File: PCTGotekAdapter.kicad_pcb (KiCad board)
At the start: 2 copper layers, 114.3 x 55.9 mm, 21 parts, among them J1 Conn_02x17_Odd_Even, J2 Conn_2Rows-19Pins, J3 Conn_2Rows-19Pins, J4 Conn_02x17_Odd_Even, J5 Conn_01x04_Pin, J6 Conn_01x04_Pin, U1 SN74LS138N, U2 SN7407N

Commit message: First pass at REV B
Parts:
- removed J3: Conn_2Rows-19Pins, Connector_PinHeader_2.54mm:PinHeader_2x10_P2.54mm_Vertical
- moved R3 130.2 mm to (175.3, 99.1), turned to 90 degrees
- moved U1 128.1 mm to (189.4, 87.6), turned to 180 degrees
- moved R4 121.5 mm to (162.6, 99.1)
- moved H1 108.3 mm to (130.4, 77.9)
- moved H2 107.8 mm to (130.4, 118.5)
- moved J2 107.0 mm to (203.2, 109.2), turned to 180 degrees
- moved TP1 106.3 mm to (128.1, 96.5)
- moved J5 106.0 mm to (127.1, 90.0)
- moved J6 105.0 mm to (127.1, 109.2)
- moved J1 103.1 mm to (182.9, 116.8)
- moved J4 102.7 mm to (182.9, 104.1)
- moved TP2 101.3 mm to (133.2, 96.5)
- moved TP3 98.8 mm to (138.2, 96.5)
- moved R1 95.0 mm to (169.0, 99.1), turned to 90 degrees
- moved C2 94.1 mm to (182.5, 96.5), turned to 180 degrees
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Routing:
- net +5V: track 278.0 -> 140.7 mm, vias 3 -> 1
- net Net-(J1-Pin_16): track 159.0 -> 31.6 mm
- net Net-(J1-Pin_24): track 120.5 -> 32.7 mm
- net Net-(J2-Pin_17): track 99.3 -> 11.9 mm, vias 2 -> 0
- net Net-(J1-Pin_20): track 107.3 -> 42.2 mm, vias 0 -> 2
- net Net-(J2-Pin_4): track 85.1 -> 21.1 mm
- net Net-(J1-Pin_18): track 97.3 -> 40.3 mm
- net Net-(J2-Pin_9): track 62.9 -> 10.9 mm, vias 1 -> 0
- net Net-(J1-Pin_32): track 96.4 -> 45.9 mm
- net Net-(J1-Pin_26): track 121.4 -> 86.7 mm, vias 2 -> 1
- net Net-(J1-Pin_22): track 89.9 -> 55.9 mm, vias 2 -> 0
- net Net-(J2-Pin_5): track 28.4 -> 54.0 mm, vias 0 -> 4
- net Net-(J1-Pin_30): track 121.3 -> 97.1 mm
- net Net-(J2-Pin_12): track 35.8 -> 59.9 mm, vias 0 -> 3
- net Net-(J2-Pin_16): track 26.0 -> 47.3 mm, vias 0 -> 1
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- added copper zone on In1.Cu, net GND
- added copper zone on In2.Cu, net GND
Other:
- board size 114.3 x 55.9 mm -> 86.4 x 50.8 mm
- copper layers 2 -> 4
- board text added: "Connect Me to Your PC Transporter"
- board text added: "Copyright ©️ 2023 / CC BY SA"
- board text added: "LOT JLCJLCJLCJLC"
- board text added: "MS DOS Drive Connectors Maximum 2 drives - addressed by jumpers Power Performance Not Guaranteed"
- board text added: "PC Transporter GoDrive"
- board text added: "REV B"
- board text removed: "MS DOS Drive Connectors Maximum 2 drives - addressed by jumpers"
- board text removed: "PC Transporter Connectors Maximum 1 Connection"
- board text removed: "PC Transporter to MS DOS Drive Adapter"
- board text removed: "REV ${Rev} LOT JLCJLCJLCJLC"

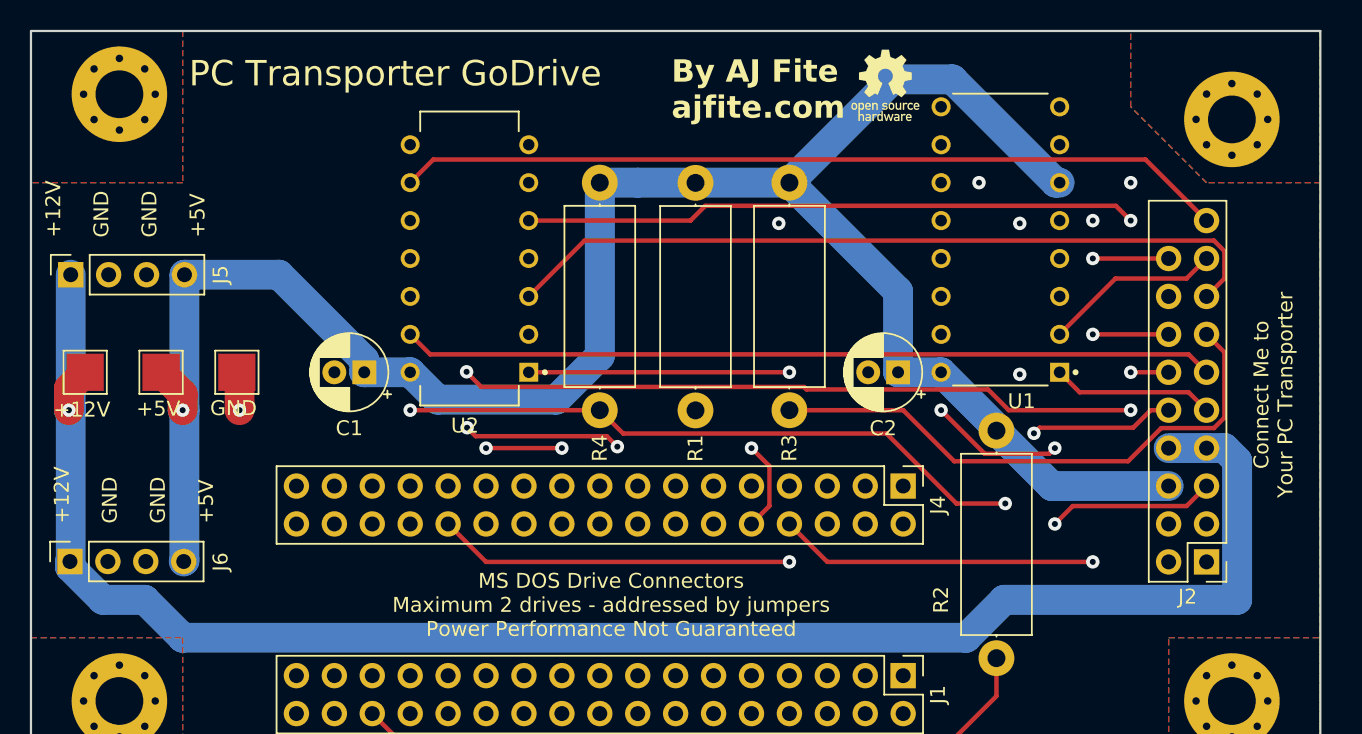
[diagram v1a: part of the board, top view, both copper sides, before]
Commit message: Remove extraneous connector from schematic
Also some silkscreen and path tweaks
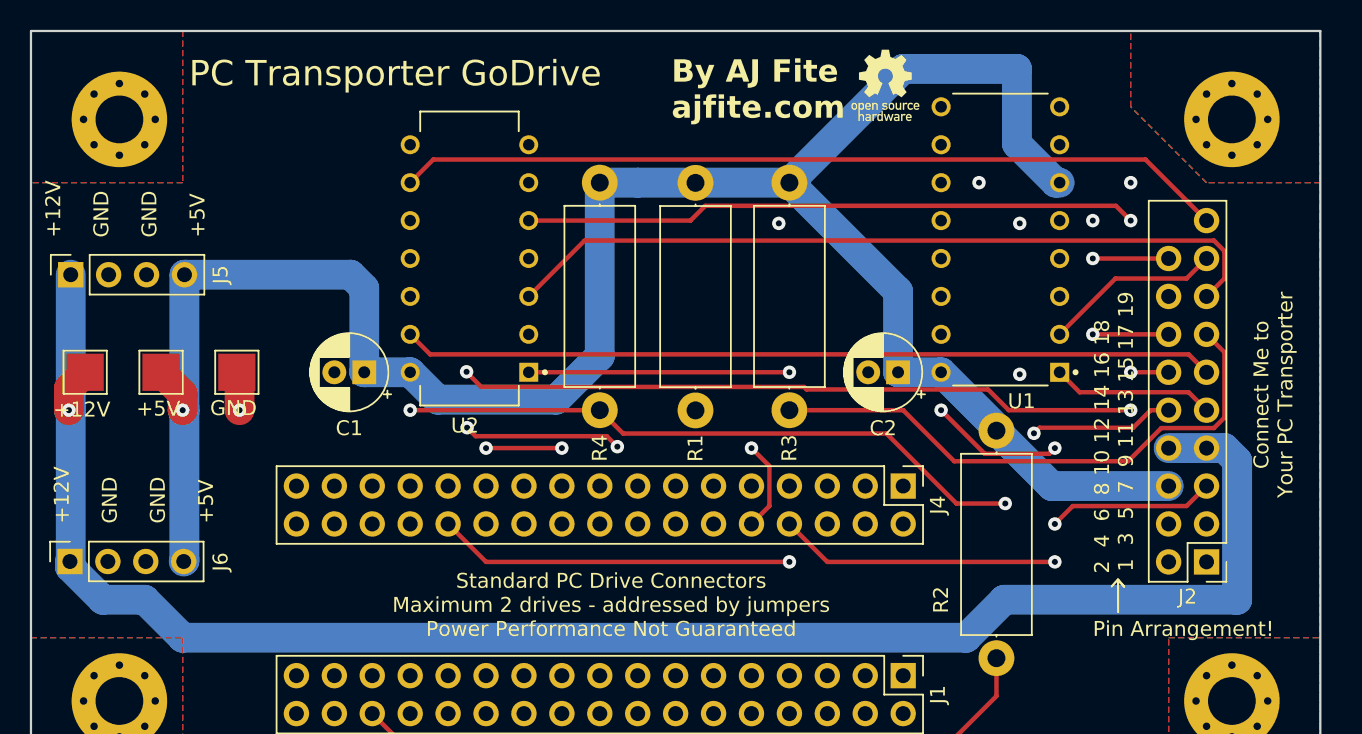
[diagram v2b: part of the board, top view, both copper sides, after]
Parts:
- moved H1 1.69 mm to (130.4, 79.6)
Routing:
- net +5V: track 140.7 -> 147.0 mm
- net Net-(J1-Pin_8): track 66.6 -> 65.1 mm
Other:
- board text added: "1 3 5 7 9 11 13 15 17 19"
- board text added: "2 4 6 8 10 12 14 16 18"
- board text added: "Pin Arrangement!"
- board text added: "Standard PC Drive Connectors Maximum 2 drives - addressed by jumpers Power Performance Not Guaranteed"
- board text removed: "MS DOS Drive Connectors Maximum 2 drives - addressed by jumpers Power Performance Not Guaranteed"
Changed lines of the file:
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@@
   )
   (footprint "MountingHole:MountingHole_3.2mm_M3_Pad_Via" (layer "F.Cu")
-    (at 130.382944 77.897056)
+    (at 130.382944 79.582944)
     (descr "Mounting Hole 3.2mm, M3")
     (tags "mounting hole 3.2mm m3")
@@
     )
     (stroke (width 0) (type solid)) (fill solid) (layer "F.SilkS"))
+  (gr_line (start 197.677346 110.868852) (end 197.272279 110.418778)
+    (stroke (width 0.15) (type default)) (layer "F.SilkS"))
   (gr_poly
     (pts
@@
     )
     (stroke (width 0) (type solid)) (fill solid) (layer "F.SilkS"))
+  (gr_line (start 197.254276 110.409777) (end 196.849209 110.859851)
+    (stroke (width 0.15) (type default)) (layer "F.SilkS"))
   (gr_poly
     (pts
@@
     )
     (stroke (width 0) (type solid)) (fill solid) (layer "F.SilkS"))
+  (gr_line (start 197.272279 110.418778) (end 197.677346 110.868852)
+    (stroke (width 0.15) (type default)) (layer "F.SilkS"))
   (gr_poly
     (pts
@@
     )
     (stroke (width 0) (type solid)) (fill solid) (layer "F.SilkS"))
+  (gr_line (start 197.28128 112.579135) (end 197.272279 110.418778)
+    (stroke (width 0.15) (type default)) (layer "F.SilkS"))
   (gr_poly
     (pts
@@
     (effects (font (size 1 1) (thickness 0.15)) (justify left bottom))
   )
+  (gr_text "1  3  5  7  9 11 13 15 17 19" (at 198.386344 109.864943 90) (layer "F.SilkS")
+    (effects (font (size 1 1) (thickness 0.15)) (justify left bottom))
+  )
+  (gr_text "Pin Arrangement!" (at 195.58 114.3) (layer "F.SilkS")
+    (effects (font (size 1 1) (thickness 0.15)) (justify left bottom))
+  )
   (gr_text "GND" (at 136.452907 99.510135) (layer "F.SilkS")
     (effects (font (size 1 1) (thickness 0.15)) (justify left bottom))
@@
     (effects (font (size 1 1) (thickness 0.15)) (justify left bottom))
   )
-  (gr_text "MS DOS Drive Connectors\nMaximum 2 drives - addressed by jumpers\nPower Performance Not Guaranteed" (at 163.320683 114.3) (layer "F.SilkS")
+  (gr_text "Standard PC Drive Connectors\nMaximum 2 drives - addressed by jumpers\nPower Performance Not Guaranteed " (at 163.320683 114.3) (layer "F.SilkS")
     (effects (font (size 1 1) (thickness 0.15)) (justify bottom))
   )
+  (gr_text "2  4  6  8 10 12 14 16 18" (at 196.789241 109.999328 90) (layer "F.SilkS")
+    (effects (font (size 1 1) (thickness 0.15)) (justify left bottom))
+  )
   (gr_text "PC Transporter GoDrive" (at 135.040285 77.508604) (layer "F.SilkS")
     (effects (font (size 1.7 1.7) (thickness 0.25)) (justify left bottom))
@@
   (segment (start 200.66 104.14) (end 192.837835 104.14) (width 2) (layer "B.Cu") (net 11))
   (segment (start 134.62 99.06) (end 134.741518 99.181518) (width 2) (layer "B.Cu") (net 11))
-  (segment (start 193.102153 83.82) (end 186.182153 76.9) (width 2) (layer "B.Cu") (net 11))
-  (segment (start 193.36 83.82) (end 193.102153 83.82) (width 2) (layer "B.Cu") (net 11))
   (segment (start 149.86 96.52) (end 146.78 96.52) (width 2) (layer "B.Cu") (net 11))
+  (segment (start 146.78 96.52) (end 146.78 90.9) (width 2) (layer "B.Cu") (net 11))
+  (segment (start 146.78 90.9) (end 145.865866 89.985866) (width 2) (layer "B.Cu") (net 11))
   (segment (start 162.56 95.43) (end 159.635 98.355) (width 2) (layer "B.Cu") (net 11))
   (segment (start 159.635 98.355) (end 151.695 98.355) (width 2) (layer "B.Cu") (net 11))
-  (segment (start 146.78 96.52) (end 146.78 95.691572) (width 2) (layer "B.Cu") (net 11))
+  (segment (start 193.36 83.82) (end 193.102153 83.82) (width 2) (layer "B.Cu") (net 11))
   (segment (start 189.127578 100.429743) (end 189.127578 100.227578) (width 2) (layer "B.Cu") (net 11))
   (segment (start 192.837835 104.14) (end 189.127578 100.429743) (width 2) (layer "B.Cu") (net 11))
+  (segment (start 190.5 81.217847) (end 190.5 76.2) (width 2) (layer "B.Cu") (net 11))
   (segment (start 162.56 83.82) (end 165.1 83.82) (width 2) (layer "B.Cu") (net 11))
+  (segment (start 145.865866 89.985866) (end 134.741518 89.985866) (width 2) (layer "B.Cu") (net 11))
   (segment (start 134.741518 98.938482) (end 134.741518 89.985866) (width 2) (layer "B.Cu") (net 11))
   (segment (start 151.695 98.355) (end 149.86 96.52) (width 2) (layer "B.Cu") (net 11))
   (segment (start 165.1 83.82) (end 175.26 83.82) (width 2) (layer "B.Cu") (net 11))
-  (segment (start 182.18 76.9) (end 175.26 83.82) (width 2) (layer "B.Cu") (net 11))
-  (segment (start 186.182153 76.9) (end 182.18 76.9) (width 2) (layer "B.Cu") (net 11))
   (segment (start 162.56 83.82) (end 162.56 95.43) (width 2) (layer "B.Cu") (net 11))
   (segment (start 134.741518 99.181518) (end 134.741518 109.143482) (width 2) (layer "B.Cu") (net 11))
-  (segment (start 146.78 95.691572) (end 141.074294 89.985866) (width 2) (layer "B.Cu") (net 11))
-  (segment (start 141.074294 89.985866) (end 134.741518 89.985866) (width 2) (layer "B.Cu") (net 11))
   (segment (start 182.537298 91.097298) (end 182.537298 96.52) (width 2) (layer "B.Cu") (net 11))
   (segment (start 182.537298 96.52) (end 185.42 96.52) (width 2) (layer "B.Cu") (net 11))
   (segment (start 175.26 83.82) (end 182.537298 91.097298) (width 2) (layer "B.Cu") (net 11))
+  (segment (start 193.102153 83.82) (end 190.5 81.217847) (width 2) (layer "B.Cu") (net 11))
   (segment (start 189.127578 100.227578) (end 185.42 96.52) (width 2) (layer "B.Cu") (net 11))
   (segment (start 134.741518 109.143482) (end 134.69 109.195) (width 2) (layer "B.Cu") (net 11))
+  (segment (start 182.88 76.2) (end 175.26 83.82) (width 2) (layer "B.Cu") (net 11))
+  (segment (start 190.5 76.2) (end 182.88 76.2) (width 2) (layer "B.Cu") (net 11))
   (segment (start 134.62 99.06) (end 134.741518 98.938482) (width 2) (layer "B.Cu") (net 11))
   (segment (start 185.42 78.74) (end 166.44 97.72) (width 0.3) (layer "In1.Cu") (net 12))
@@
   (segment (start 149.86 93.98) (end 151.2 95.32) (width 0.3) (layer "F.Cu") (net 25))
   (segment (start 151.2 95.32) (end 202 95.32) (width 0.3) (layer "F.Cu") (net 25))
-  (segment (start 195.58 109.22) (end 177.8 109.22) (width 0.3) (layer "F.Cu") (net 29))
   (segment (start 200.66 93.98) (end 195.58 93.98) (width 0.3) (layer "F.Cu") (net 29))
+  (segment (start 193.04 109.22) (end 177.8 109.22) (width 0.3) (layer "F.Cu") (net 29))
   (segment (start 177.8 109.22) (end 175.26 106.68) (width 0.3) (layer "F.Cu") (net 29))
   (via (at 195.58 93.98) (size 0.9) (drill 0.4) (layers "F.Cu" "B.Cu") (net 29))
-  (via (at 195.58 109.22) (size 0.9) (drill 0.4) (layers "F.Cu" "B.Cu") (net 29))
-  (segment (start 195.58 109.22) (end 195.58 99.06) (width 0.3) (layer "In1.Cu") (net 29))
+  (via (at 193.04 109.22) (size 0.9) (drill 0.4) (layers "F.Cu" "B.Cu") (net 29))
+  (segment (start 195.58 106.68) (end 195.58 93.98) (width 0.3) (layer "In1.Cu") (net 29))
   (segment (start 172.222943 105.34) (end 173.92 105.34) (width 0.3) (layer "In1.Cu") (net 29))
   (segment (start 168.970731 99.073586) (end 171.52 101.622855) (width 0.3) (layer "In1.Cu") (net 29))
@@
   (segment (start 174.06 107.88) (end 175.26 106.68) (width 0.3) (layer "In1.Cu") (net 29))
   (segment (start 171.52 104.637057) (end 172.222943 105.34) (width 0.3) (layer "In1.Cu") (net 29))
+  (segment (start 193.04 109.22) (end 195.58 106.68) (width 0.3) (layer "In1.Cu") (net 29))
   (segment (start 171.52 101.622855) (end 171.52 104.637057) (width 0.3) (layer "In1.Cu") (net 29))
-  (segment (start 195.58 99.06) (end 195.58 93.98) (width 0.3) (layer "In1.Cu") (net 29))
   (segment (start 173.92 105.34) (end 175.26 106.68) (width 0.3) (layer "In1.Cu") (net 29))
   (segment (start 204.4 99.557057) (end 203.697057 100.26) (width 0.3) (layer "F.Cu") (net 31))

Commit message: Additional updates to the PCB and silk
This will be ready for printing extremely soon
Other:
- board text added: "12V"
- board text added: "5V"
- board text added: "Cut these traces if you want to use external power for the GoDrive"
- board text added: "Ground Pins!"
- board text added: "I'm designed for M3 screws!"
- board text added: "Standard PC Drive Connectors Maximum 2 drives - addressing done on drive Power Performance Not Guaranteed (but you should be fine)"
- board text removed: "Standard PC Drive Connectors Maximum 2 drives - addressed by jumpers Power Performance Not Guaranteed"

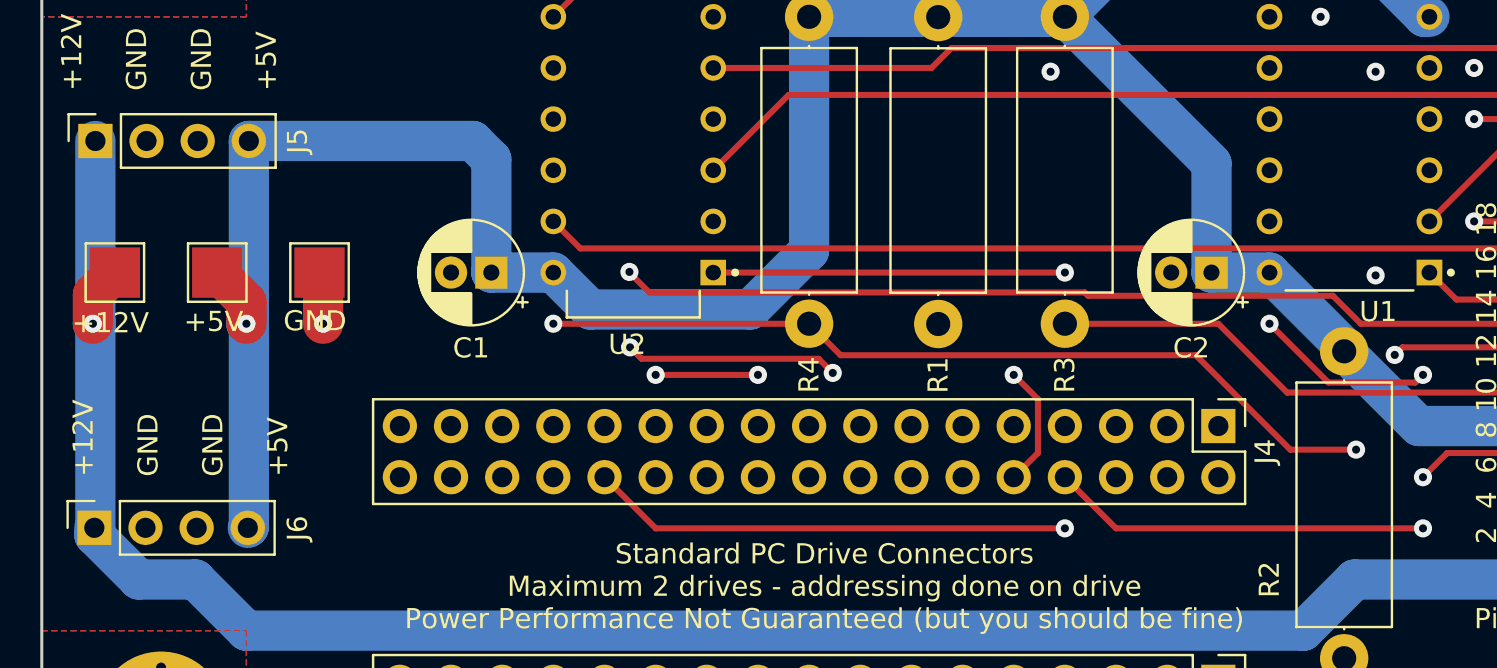
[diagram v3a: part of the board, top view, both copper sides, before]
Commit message: Silkscreen and routing updates, schematic fixes
Also ignored .zip files
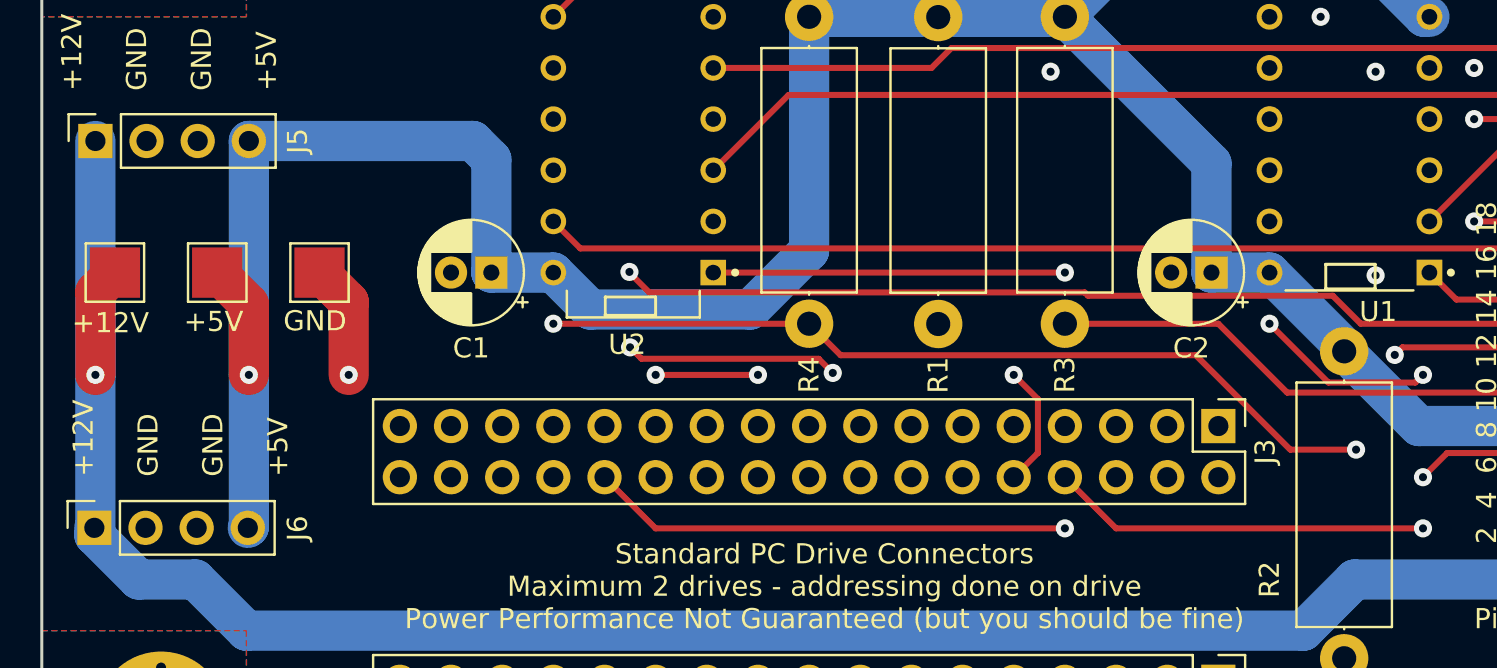
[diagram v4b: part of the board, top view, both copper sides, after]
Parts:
- renumbered J4 to J3
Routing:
- net +5V: track 147.0 -> 149.5 mm
- net +12V: track 118.1 -> 120.5 mm
- net GND: track 333.3 -> 334.1 mm
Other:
- board text added: "You can also simply not connect the boxed pins if you want to use external power"
